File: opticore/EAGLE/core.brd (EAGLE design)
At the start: 91 x 77 mm, 72 parts, among them IC1 LM2596T, J1 POWER_JACKSLT, J2 POWER_JACKSLT, Q1 2N3904, Q2 2N3904, Q3 2N3904, Q4 2N3904, Q5 2N3904, Q6 2N3904, Q7 2N3904, X1 FFKV8

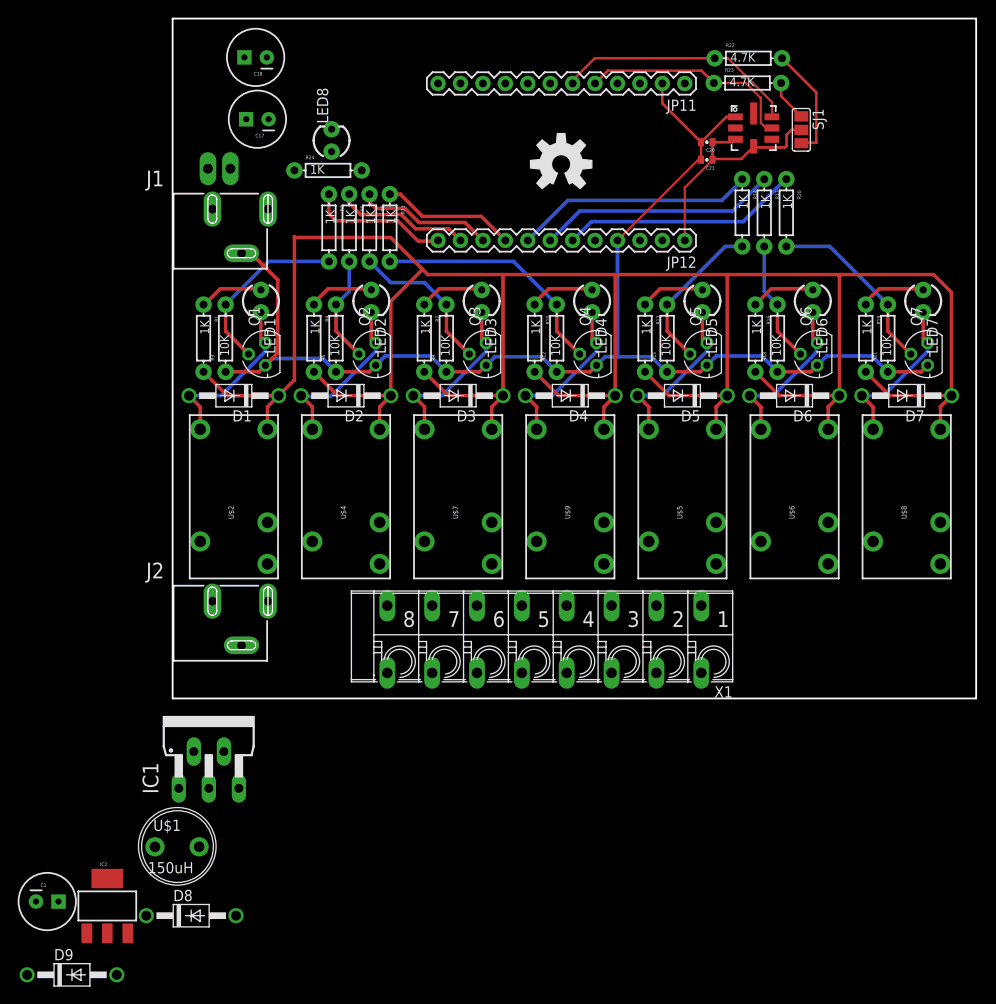
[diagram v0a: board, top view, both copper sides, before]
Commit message: Placed and Routed new 24VAC to 5VDC
Hopefully this works as expected. Horray for Rev 1!

Signed-off-by: Scott Lerner <scottphiliplerner@gmail.com>
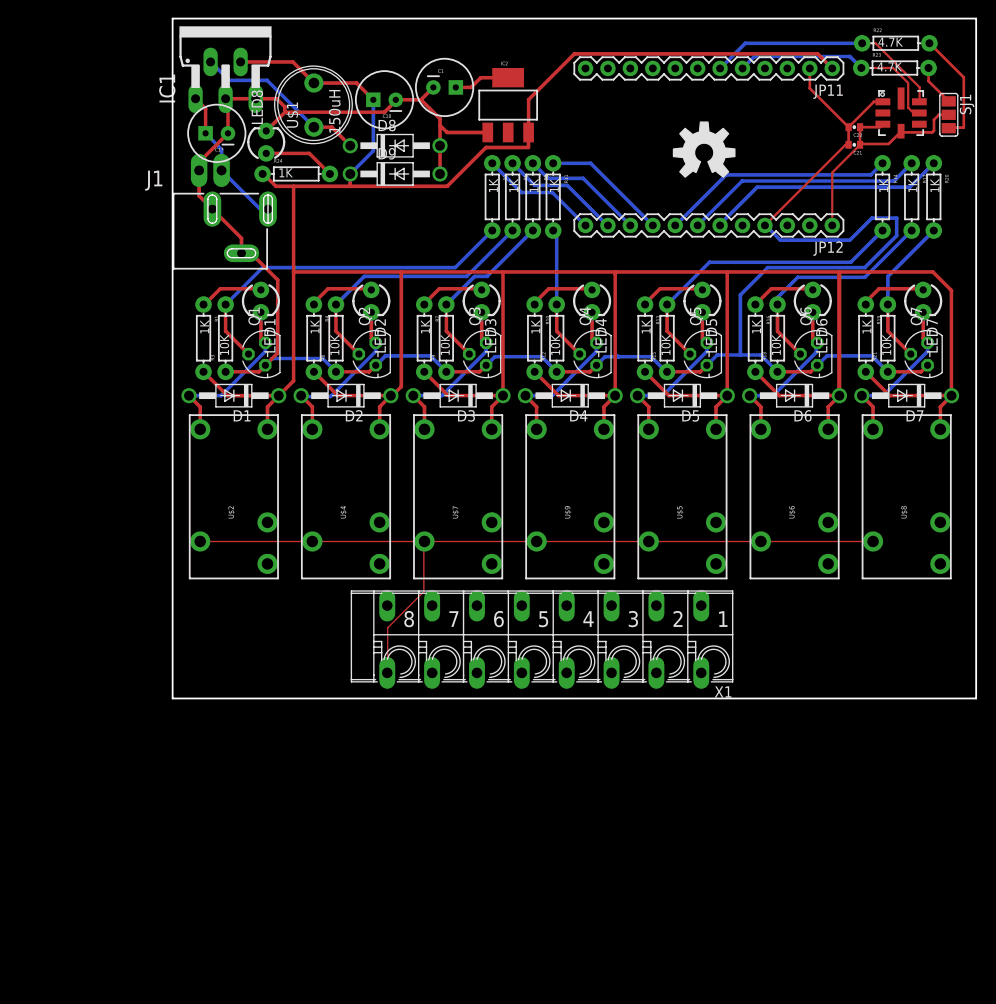
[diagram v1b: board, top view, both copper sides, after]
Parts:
- removed J2: POWER_JACKSLT, SparkFun-Connectors:POWER_JACK_SLOT
- moved C1 102.6 mm to (30.8, 69.2)
- moved IC2 101.4 mm to (38.0, 67.2)
- moved D9 97.8 mm to (25.2, 59.4)
- moved D8 90.2 mm to (25.2, 62.6)
- moved U$1 85.4 mm to (16.0, 67.2), turned to 90 degrees
- moved IC1 78.1 mm to (6.00, 73.0)
- moved R2 18.8 mm to (36.2, 56.8)
- moved R11 18.8 mm to (43.1, 56.8)
- moved R5 18.8 mm to (38.5, 56.8)
- moved R8 18.8 mm to (40.8, 56.8)
- moved R17 16.8 mm to (83.7, 56.8)
- moved R20 16.8 mm to (86.2, 56.8)
- moved C20 16.8 mm to (77.2, 64.7)
- moved C21 16.8 mm to (77.2, 62.7)
- moved JP11 16.8 mm to (74.7, 71.3)
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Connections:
- removed net +24V: J2.PWR, X1.1A, X1.2A, X1.3A, X1.4A, X1.5A, X1.6A, X1.7A
- new net N$11: X1.6A
- new net N$12: X1.1A
- new net N$13: X1.2A
- new net N$14: X1.3A
- new net N$15: X1.4A
- new net N$16: X1.5A
- new net N$17: X1.7A
- net MAIN: no longer J2.GND@1, J2.GND@2
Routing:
- net 5V: track 280.2 -> 401.5 mm
- net GND: track 146.1 -> 243.8 mm
- net MAIN: track 0.00 -> 92.8 mm
- net N$24: track 20.4 -> 40.4 mm
- net N$10: track 0.00 -> 19.8 mm
- net N$20: track 12.2 -> 30.2 mm
- net N$23: track 17.9 -> 34.6 mm
- net N$37: track 0.00 -> 16.4 mm
- net N$36: track 27.6 -> 15.2 mm
- net N$27: track 13.9 -> 25.8 mm
- net N$39: track 0.00 -> 8.18 mm
- net 3.3V: track 0.00 -> 6.39 mm
- net N$33: track 20.9 -> 17.2 mm
- net N$30: track 17.4 -> 20.0 mm
- net RELAY1: track 15.9 -> 13.5 mm
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
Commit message: Accidentally Missed these commits.
Don't know exactly what they are.
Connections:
- net N$37 renamed +24V
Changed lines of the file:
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@@
 <contactref element="C1" pad="2"/>
 <wire x1="67.2084" y1="53.5178" x2="67.08" y2="53.57" width="0.1524" layer="16"/>
-<wire x1="7.8" y1="50.42" x2="7.8" y2="52.12" width="0.4064" layer="1"/>
-<wire x1="7.8" y1="52.12" x2="4.5" y2="55.42" width="0.4064" layer="1"/>
-<wire x1="3" y1="59.8" x2="3" y2="56.92" width="0.4064" layer="1"/>
-<wire x1="3" y1="56.92" x2="4.5" y2="55.42" width="0.4064" layer="1"/>
 <wire x1="3" y1="59.8" x2="3" y2="60.73" width="0.4064" layer="1"/>
 <wire x1="3" y1="60.73" x2="6.27" y2="64" width="0.4064" layer="1"/>
@@
 <wire x1="66.6" y1="38.9" x2="68.5" y2="37" width="0.4064" layer="16"/>
 <wire x1="68.5" y1="37" x2="68.5" y2="36.99" width="0.4064" layer="16"/>
+<wire x1="7.8" y1="50.42" x2="7.8" y2="52.12" width="0.4064" layer="16"/>
+<wire x1="7.8" y1="52.12" x2="4.5" y2="55.42" width="0.4064" layer="16"/>
+<wire x1="4.5" y1="55.42" x2="3" y2="56.92" width="0.4064" layer="16"/>
+<wire x1="3" y1="56.92" x2="3" y2="59.8" width="0.4064" layer="16"/>
 </signal>
 <signal name="+3V3">
@@
 <wire x1="62" y1="53.7" x2="62" y2="53.57" width="0.4064" layer="16"/>
 </signal>
-<signal name="N$37">
-<contactref element="J1" pad="PWR"/>
-<contactref element="JP10" pad="2"/>
-<contactref element="C17" pad="1"/>
-<contactref element="IC1" pad="1"/>
-<wire x1="10.8" y1="55.42" x2="9.92" y2="55.42" width="0.4064" layer="16"/>
-<wire x1="9.92" y1="55.42" x2="5.54" y2="59.8" width="0.4064" layer="16"/>
-<wire x1="5.54" y1="59.8" x2="5.54" y2="62.19" width="0.4064" layer="16"/>
-<wire x1="5.54" y1="62.19" x2="3.73" y2="64" width="0.4064" layer="16"/>
-<wire x1="3.73" y1="64" x2="3.73" y2="66.7864" width="0.4064" layer="1"/>
-<wire x1="3.73" y1="66.7864" x2="2.5964" y2="67.92" width="0.4064" layer="1"/>
-</signal>
 <signal name="N$39">
 <contactref element="R24" pad="P$2"/>
@@
 <contactref element="X1" pad="7A"/>
 </signal>
+<signal name="+24V">
+<contactref element="J1" pad="PWR"/>
+<contactref element="JP10" pad="2"/>
+<contactref element="C17" pad="1"/>
+<contactref element="IC1" pad="1"/>
+<wire x1="10.8" y1="55.42" x2="9.92" y2="55.42" width="0.4064" layer="16"/>
+<wire x1="9.92" y1="55.42" x2="5.54" y2="59.8" width="0.4064" layer="16"/>
+<wire x1="5.54" y1="59.8" x2="5.54" y2="62.19" width="0.4064" layer="16"/>
+<wire x1="5.54" y1="62.19" x2="3.73" y2="64" width="0.4064" layer="16"/>
+<wire x1="3.73" y1="64" x2="3.73" y2="66.7864" width="0.4064" layer="1"/>
+<wire x1="3.73" y1="66.7864" x2="2.5964" y2="67.92" width="0.4064" layer="1"/>
+</signal>
 </signals>
